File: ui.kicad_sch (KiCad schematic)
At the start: 7 parts, among them J18 Conn_01x14_MountingPin, J19 Conn_01x14_MountingPin, Q9 IRLML2502

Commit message: Final checks and cleanup
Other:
- note added: "Display FPC connection"
- moved on the sheet: BZ1, J18, J19, Q9, R19, R27, R29

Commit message: Fix revision
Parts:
- J18, J19: Mouser Part Number (none) -> 653-XF2M-1415-1A
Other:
- title: openautolab - Mainboard -> openautolab - Alternative Mainboard
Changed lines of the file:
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@@
   (paper "A4")
   (title_block
-    (title "openautolab - Mainboard")
+    (title "openautolab - Alternative Mainboard")
     (date "2024-04-03")
-    (rev "2.0")
+    (rev "1")
   )
   (junction (at 209.55 92.71) (diameter 0) (color 0 0 0 0)
@@
     )
     (property "Datasheet" "~" (at 63.5 93.98 0)
+      (effects (font (size 1.27 1.27)) hide)
+    )
+    (property "Mouser Part Number" "653-XF2M-1415-1A" (at 63.5 93.98 0)
       (effects (font (size 1.27 1.27)) hide)
     )
@@
       (effects (font (size 1.27 1.27)) hide)
     )
+    (property "Mouser Part Number" "653-XF2M-1415-1A" (at 128.905 90.805 0)
+      (effects (font (size 1.27 1.27)) hide)
+    )

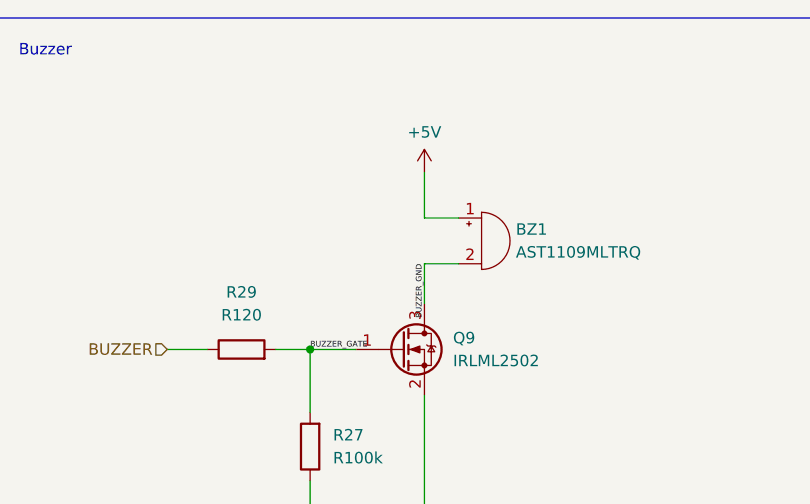
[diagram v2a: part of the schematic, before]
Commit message: - Start Rev 2 - Add 5k1 resistor (R30) parallel to piezo (BZ1) - Remove redundant 5V wire from bottom at buck converter (U2)
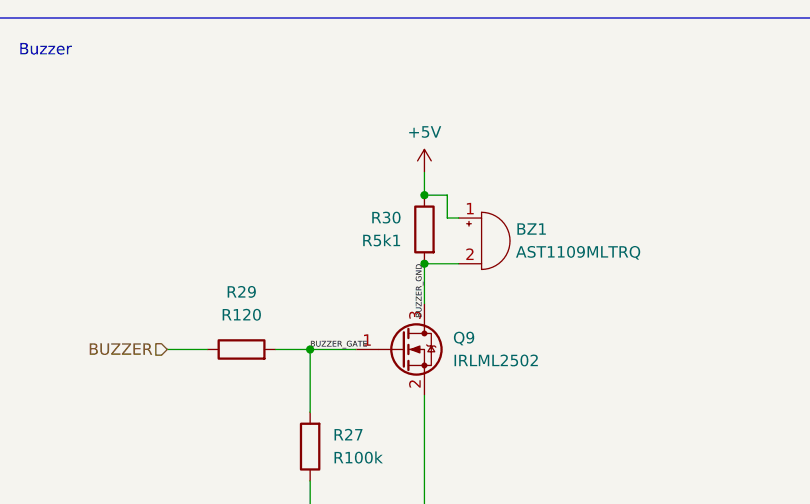
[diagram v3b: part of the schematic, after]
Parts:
- added R30: R5k1, Resistor_SMD:R_0603_1608Metric, symbol Device:R
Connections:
- net +5V: now also R30.1
- net BUZZER_GND: now also R30.2
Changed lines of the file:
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@@
     (title "openautolab - Alternative Mainboard")
     (date "2024-04-03")
-    (rev "1")
+    (rev "2")
+  )
+  (junction (at 222.25 75.565) (diameter 0) (color 0 0 0 0)
   )
   (junction (at 209.55 92.71) (diameter 0) (color 0 0 0 0)
+  )
+  (junction (at 222.25 83.185) (diameter 0) (color 0 0 0 0)
   )
   (no_connect (at 58.42 76.2))
@@
     (stroke (width 0) (type default))
   )
-  (wire (pts (xy 222.25 78.105) (xy 222.25 73.025))
-    (stroke (width 0) (type default))
-  )
   (wire (pts (xy 120.015 100.965) (xy 123.825 100.965))
     (stroke (width 0) (type default))
@@
     (stroke (width 0) (type default))
   )
-  (wire (pts (xy 226.06 78.105) (xy 222.25 78.105))
-    (stroke (width 0) (type default))
-  )
   (wire (pts (xy 120.015 90.805) (xy 123.825 90.805))
     (stroke (width 0) (type default))
@@
     (stroke (width 0) (type default))
   )
+  (wire (pts (xy 222.25 73.025) (xy 222.25 75.565))
+    (stroke (width 0) (type default))
+  )
   (wire (pts (xy 42.545 104.14) (xy 58.42 104.14))
     (stroke (width 0) (type default))
@@
     (stroke (width 0) (type default))
   )
+  (wire (pts (xy 224.79 78.105) (xy 224.79 75.565))
+    (stroke (width 0) (type default))
+  )
+  (wire (pts (xy 224.79 75.565) (xy 222.25 75.565))
+    (stroke (width 0) (type default))
+  )
   (wire (pts (xy 123.825 108.585) (xy 123.825 123.825))
     (stroke (width 0) (type default))
@@
   )
   (wire (pts (xy 120.015 95.885) (xy 123.825 95.885))
+    (stroke (width 0) (type default))
+  )
+  (wire (pts (xy 226.06 78.105) (xy 224.79 78.105))
     (stroke (width 0) (type default))
   )
@@
         )
       )
+    )
+  )
+  (symbol (lib_id "Device:R") (at 222.25 79.375 0) (mirror y) (unit 1)
+    (in_bom yes) (on_board yes) (dnp no)
+    (property "Reference" "R30" (at 219.71 78.105 0)
+      (effects (font (size 1.27 1.27)) (justify left))
+    )
+    (property "Value" "R5k1" (at 219.71 80.645 0)
+      (effects (font (size 1.27 1.27)) (justify left))
+    )
+    (property "Footprint" "Resistor_SMD:R_0603_1608Metric" (at 224.028 79.375 90)
+      (effects (font (size 1.27 1.27)) hide)
+    )
+    (property "Datasheet" "~" (at 222.25 79.375 0)
+      (effects (font (size 1.27 1.27)) hide)
+    )
+    (property "Mouser Part Number" "667-ERJ-3EKF5101V" (at 222.25 79.375 0)
+      (effects (font (size 1.27 1.27)) hide)
+    )
+    (pin "1")
+    (pin "2")
+    (instances
+      (project "mainboard"
+        (path "/613f8c39-c37c-4981-8911-5138d36a7959/e16aa466-f341-4735-929a-c85f813defce"
+          (reference "R30") (unit 1)
+        )
+      )
